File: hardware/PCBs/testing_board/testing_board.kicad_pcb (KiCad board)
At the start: 2 copper layers, 100.6 x 99.1 mm, 75 parts, among them J1 Conn_01x04, J16 Conn_01x04, J2 Conn_01x04, J3 Conn_01x04, J4 Conn_01x04, J5 Conn_01x04, J6 Conn_01x04, J7 Conn_01x04, J8 Conn_01x04, J9 Conn_01x04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

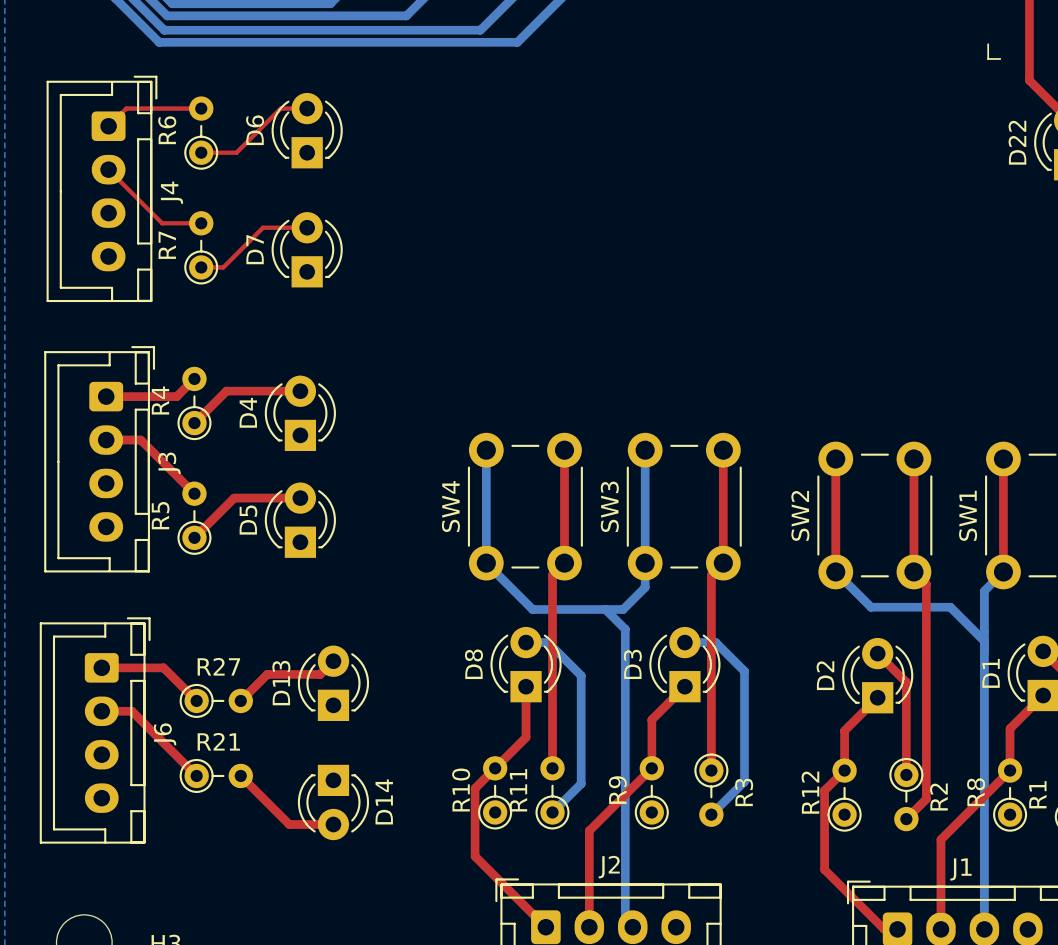
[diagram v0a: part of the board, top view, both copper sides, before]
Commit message: update testing board and its bom
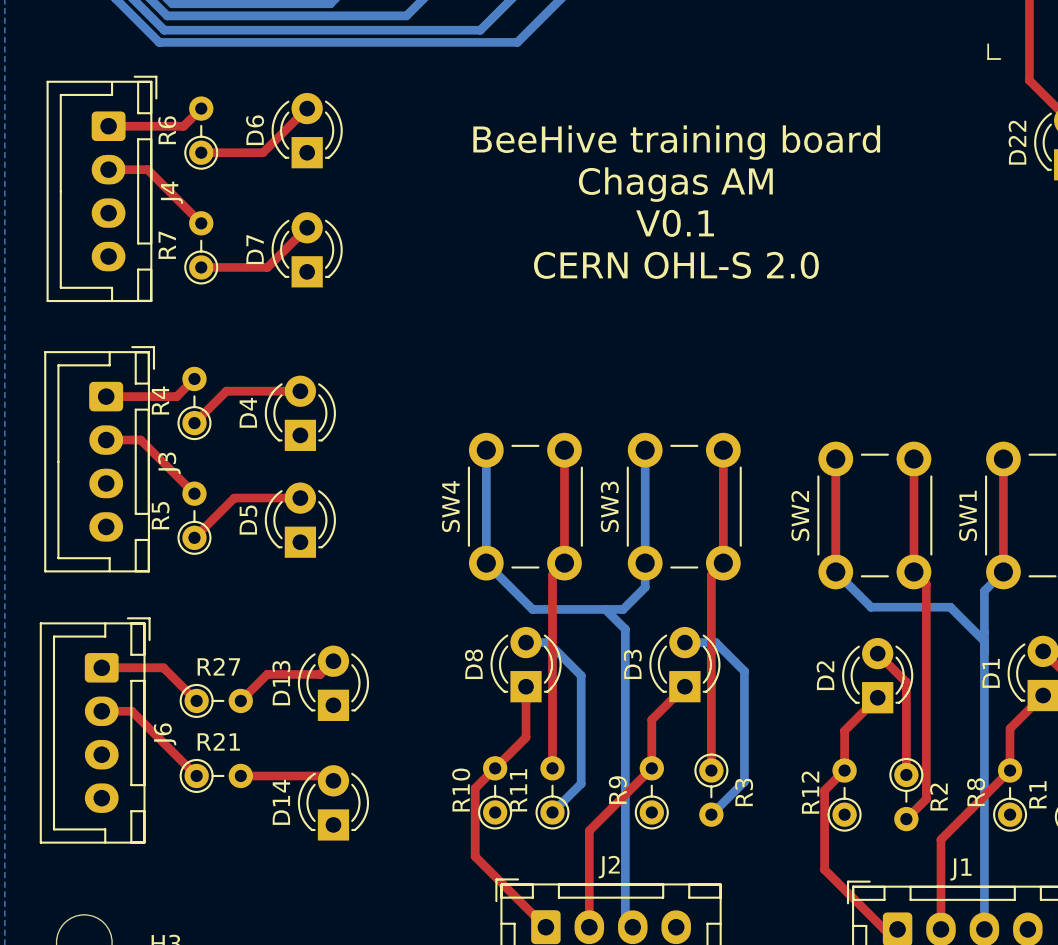
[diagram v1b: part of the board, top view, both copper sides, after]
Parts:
- moved D14 2.57 mm to (56.2, 107.5), turned to 90 degrees
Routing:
- net Net-(D14-Pad2): track 6.49 -> 5.45 mm
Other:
- board text added: "BeeHive training board Chagas AM V0.1 CERN OHL-S 2.0"
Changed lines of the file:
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@@
   )
   (footprint "LED_THT:LED_D3.0mm" (layer "F.Cu")
-    (at 56.25 104.96 -90)
+    (at 56.25 107.525 90)
     (descr "LED, diameter 3.0mm, 2 pins")
     (tags "LED diameter 3.0mm 2 pins")
@@
     (fp_arc (start -0.23 -1.16619) (mid 3.17 0.000452) (end -0.230555 1.165476) (layer "F.Fab") (width 0.1))
     (fp_circle (center 1.27 0) (end 2.77 0) (layer "F.Fab") (width 0.1) (fill none))
-    (pad "1" thru_hole rect locked (at 0 0 270) (size 1.8 1.8) (drill 0.9) (layers *.Cu *.Mask)
+    (pad "1" thru_hole rect locked (at 0 0 90) (size 1.8 1.8) (drill 0.9) (layers *.Cu *.Mask)
       (net 6 "GND") (pinfunction "K") (pintype "passive"))
-    (pad "2" thru_hole circle locked (at 2.54 0 270) (size 1.8 1.8) (drill 0.9) (layers *.Cu *.Mask)
+    (pad "2" thru_hole circle locked (at 2.54 0 90) (size 1.8 1.8) (drill 0.9) (layers *.Cu *.Mask)
       (net 18 "Net-(D14-Pad2)") (pinfunction "A") (pintype "passive"))
     (model "${KISYS3DMOD}/LED_THT.3dshapes/LED_D3.0mm.wrl"
@@
   (gr_line (start 36.83 119.38) (end 137.414 119.38) (layer "Edge.Cuts") (width 0.05))
   (gr_line (start 36.83 21.336) (end 36.83 119.38) (layer "Edge.Cuts") (width 0.05))
+  (gr_text "BeeHive training board\nChagas AM\nV0.1\nCERN OHL-S 2.0 " (at 76 71.75) (layer "F.SilkS")
+    (effects (font (size 1.5 1.5) (thickness 0.3)))
+  )
   (dimension (type aligned) (layer "Eco1.User")
     (pts (xy 36.83 20.32) (xy 36.83 119.38))
@@
   (segment (start 54.346 88.714) (end 50.536 88.714) (width 0.5) (layer "F.Cu") (net 8))
   (segment (start 50.536 88.714) (end 48.25 91) (width 0.5) (layer "F.Cu") (net 8))
-  (segment (start 48.641 68.834) (end 50.673 68.834) (width 0.25) (layer "F.Cu") (net 9))
-  (segment (start 53.213 66.294) (end 54.737 66.294) (width 0.25) (layer "F.Cu") (net 9))
-  (segment (start 50.673 68.834) (end 53.213 66.294) (width 0.25) (layer "F.Cu") (net 9))
-  (segment (start 48.641 75.438) (end 49.911 75.438) (width 0.25) (layer "F.Cu") (net 10))
-  (segment (start 49.911 75.438) (end 52.197 73.152) (width 0.25) (layer "F.Cu") (net 10))
-  (segment (start 52.197 73.152) (end 54.737 73.152) (width 0.25) (layer "F.Cu") (net 10))
+  (segment (start 52.197 68.834) (end 54.737 66.294) (width 0.5) (layer "F.Cu") (net 9))
+  (segment (start 48.641 68.834) (end 52.197 68.834) (width 0.5) (layer "F.Cu") (net 9))
+  (segment (start 48.641 75.438) (end 52.451 75.438) (width 0.5) (layer "F.Cu") (net 10))
+  (segment (start 52.451 75.438) (end 54.737 73.152) (width 0.5) (layer "F.Cu") (net 10))
   (segment (start 64.405999 109.339999) (end 68.477 113.411) (width 0.5) (layer "F.Cu") (net 11))
   (segment (start 67.334 99.568) (end 67.334 102.489) (width 0.5) (layer "F.Cu") (net 11))
@@
   (segment (start 42.915 98.483) (end 46.471 98.483) (width 0.5) (layer "F.Cu") (net 17))
   (segment (start 46.471 98.483) (end 48.376 100.388) (width 0.5) (layer "F.Cu") (net 17))
-  (segment (start 56.25 107.5) (end 53.71 107.5) (width 0.5) (layer "F.Cu") (net 18))
-  (segment (start 53.71 107.5) (end 50.916 104.706) (width 0.5) (layer "F.Cu") (net 18))
+  (segment (start 50.916 104.706) (end 55.971 104.706) (width 0.5) (layer "F.Cu") (net 18))
+  (segment (start 55.971 104.706) (end 56.25 104.985) (width 0.5) (layer "F.Cu") (net 18))
   (segment (start 72.58 54.2) (end 72.58 49.505) (width 0.5) (layer "F.Cu") (net 19))
   (segment (start 72.58 49.505) (end 72.275 49.2) (width 0.5) (layer "F.Cu") (net 19))
@@
   (segment (start 42.916 82.872) (end 47.234 82.872) (width 0.5) (layer "F.Cu") (net 24))
   (segment (start 47.234 82.872) (end 48.25 81.856) (width 0.5) (layer "F.Cu") (net 24))
-  (segment (start 44.323 66.294) (end 43.307 67.31) (width 0.25) (layer "F.Cu") (net 25))
-  (segment (start 48.641 66.294) (end 44.323 66.294) (width 0.25) (layer "F.Cu") (net 25))
-  (segment (start 46.395 72.898) (end 43.307 69.81) (width 0.25) (layer "F.Cu") (net 26))
-  (segment (start 48.641 72.898) (end 46.395 72.898) (width 0.25) (layer "F.Cu") (net 26))
+  (segment (start 47.625 67.31) (end 48.641 66.294) (width 0.5) (layer "F.Cu") (net 25))
+  (segment (start 43.307 67.31) (end 47.625 67.31) (width 0.5) (layer "F.Cu") (net 25))
+  (segment (start 43.307 69.81) (end 45.553 69.81) (width 0.5) (layer "F.Cu") (net 26))
+  (segment (start 45.553 69.81) (end 48.641 72.898) (width 0.5) (layer "F.Cu") (net 26))
   (segment (start 117.679999 109.847999) (end 120.652001 109.847999) (width 0.5) (layer "B.Cu") (net 27))
   (segment (start 120.652001 109.847999) (end 125.847999 104.652001) (width 0.5) (layer "B.Cu") (net 27))
